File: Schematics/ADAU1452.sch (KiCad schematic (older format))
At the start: 99 parts, among them CN201 COAX, P201 CONN_2x1, P203 CONN_6X2, P204 CONN_6x1, SW202 SWITCH, U201 ADAU1452WBCPZ, U202 ADM13307-5ARZ, U203 25AA1024, X201 24M576

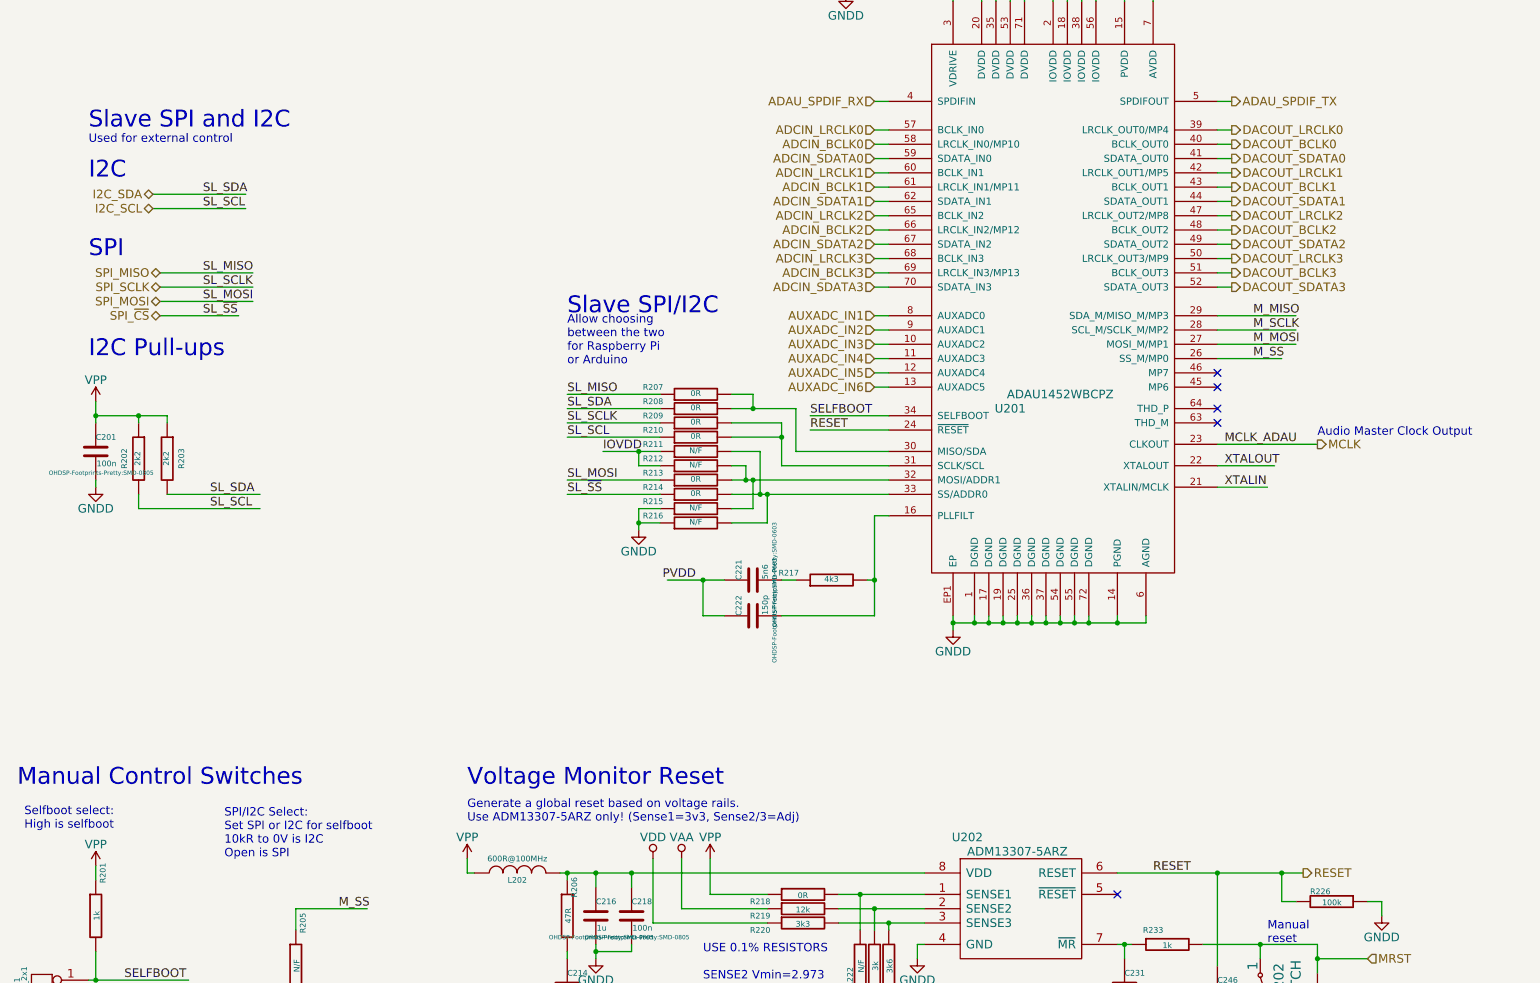
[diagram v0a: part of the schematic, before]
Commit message: WIP
Removed Slave SPI as only really need I2C
Should free up some space on the board.
May look to change U.fl to SMA
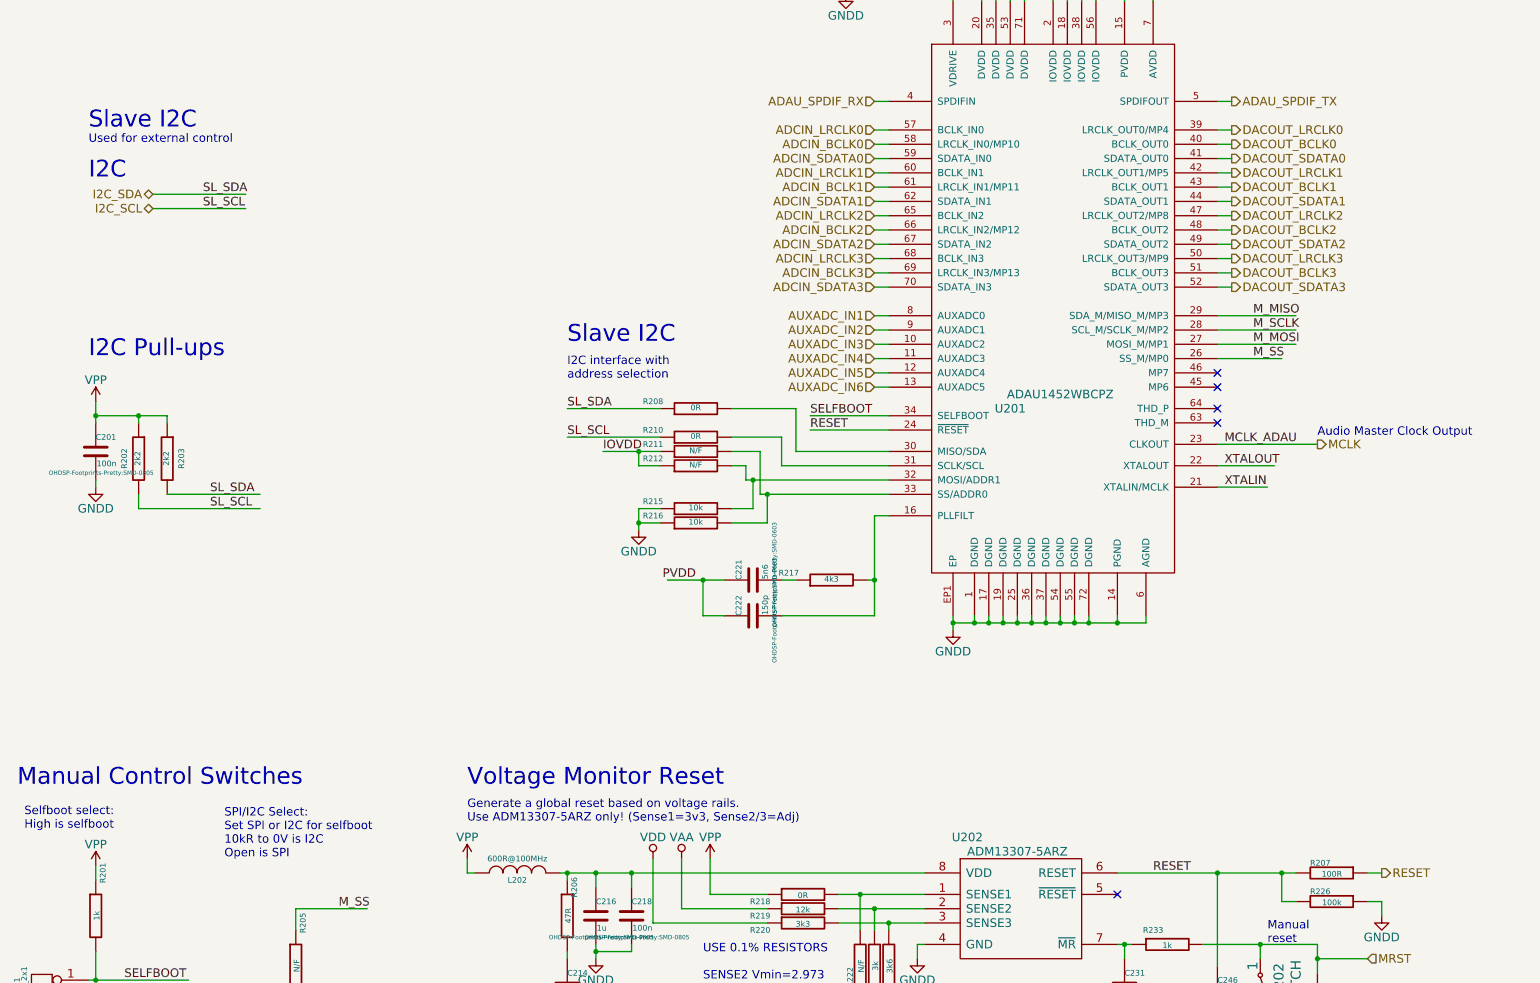
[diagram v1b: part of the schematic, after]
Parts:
- removed R209, R213, R214: 0R, OHDSP-Footprints-Pretty:SMD-0805, symbol R
- R207: value 0R -> 100R
- R215, R216: value N/F -> 10k
- U203: footprint OHDSP-Footprints-Pretty:IC_DIP_8 -> OHDSP-Footprints-Pretty:IC_SOIC_8
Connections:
- net labels removed: SL_MISO, SL_MOSI, SL_SCLK, SL_~SS, SPI_MISO, SPI_MOSI, SPI_SCLK, SPI_~CS
- wire segments 327 -> 317
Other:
- note added: "I2C interface with \naddress selection"
- note added: "Slave I2C"
- note removed: "Allow choosing\nbetween the two\nfor Raspberry Pi\nor Arduino"
- note removed: "SPI"
- note removed: "Slave SPI and I2C"
- note removed: "Slave SPI/I2C"
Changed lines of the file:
@@
 Text Notes 11450 4400 0    118  ~ 0
 SPI EEPROM
-Text Label 4500 6150 0    60   ~ 0
-SL_MISO
-Text Label 4500 6350 0    60   ~ 0
-SL_SCLK
-Text Label 4500 6850 0    60   ~ 0
-SL_~SS
-Text Label 4500 6750 0    60   ~ 0
-SL_MOSI
 $Comp
 L C C222
@@
 F 0 "U203" H 13940 5690 60  0000 C CNN
 F 1 "25AA1024" H 14050 5600 60  0000 C CNN
-F 2 "OHDSP-Footprints-Pretty:IC_DIP_8" H 13700 5550 60  0001 C CNN
+F 2 "OHDSP-Footprints-Pretty:IC_SOIC_8" H 13700 5550 60  0001 C CNN
 F 3 "" H 13700 5550 60  0000 C CNN
 	1    13600 5450
@@
 F 3 "~" H 5400 6250 30  0000 C CNN
 	1    5400 6250
-	0    -1   -1   0
-$EndComp
-$Comp
-L R R207
-U 1 1 54E23425
-P 5400 6150
-F 0 "R207" V 5450 6450 40  0000 C CNN
-F 1 "0R" V 5407 6151 40  0000 C CNN
-F 2 "OHDSP-Footprints-Pretty:SMD-0805" V 5330 6150 30  0001 C CNN
-F 3 "~" H 5400 6150 30  0000 C CNN
-	1    5400 6150
-	0    -1   -1   0
-$EndComp
-$Comp
-L R R209
-U 1 1 54E23533
-P 5400 6350
-F 0 "R209" V 5450 6650 40  0000 C CNN
-F 1 "0R" V 5407 6351 40  0000 C CNN
-F 2 "OHDSP-Footprints-Pretty:SMD-0805" V 5330 6350 30  0001 C CNN
-F 3 "~" H 5400 6350 30  0000 C CNN
-	1    5400 6350
 	0    -1   -1   0
 $EndComp
@@
 Text HLabel 6650 6100 0    60   Input ~ 0
 AUXADC_IN6
-Text Label 1950 5300 0    60   ~ 0
-SL_MISO
 Text Label 1950 4750 0    60   ~ 0
 SL_SDA
-Text Label 1950 5400 0    60   ~ 0
-SL_SCLK
 Text Label 1950 4850 0    60   ~ 0
 SL_SCL
-Text Label 1950 5500 0    60   ~ 0
-SL_MOSI
-Text Label 1950 5600 0    60   ~ 0
-SL_~SS
 Text HLabel 1600 4850 0    60   BiDi ~ 0
 I2C_SCL
 Text HLabel 1600 4750 0    60   BiDi ~ 0
 I2C_SDA
-Text HLabel 1650 5300 0    60   BiDi ~ 0
-SPI_MISO
-Text HLabel 1650 5400 0    60   BiDi ~ 0
-SPI_SCLK
-Text HLabel 1650 5500 0    60   BiDi ~ 0
-SPI_MOSI
-Text HLabel 1650 5600 0    60   BiDi ~ 0
-SPI_~CS
 Text Notes 1150 4650 0    118  ~ 0
 I2C
-Text Notes 1150 5200 0    118  ~ 0
-SPI
 $Comp
 L VPP #PWR020
@@
 Allow for self boot\nUses master SPI
 Text Notes 1150 4300 0    118  ~ 0
-Slave SPI and I2C
+Slave I2C
 Text Notes 1150 4400 0    59   ~ 0
 Used for external control
-$Comp
-L R R213
-U 1 1 54E3266A
-P 5400 6750
-F 0 "R213" V 5450 7050 40  0000 C CNN
-F 1 "0R" V 5407 6751 40  0000 C CNN
-F 2 "OHDSP-Footprints-Pretty:SMD-0805" V 5330 6750 30  0001 C CNN
-F 3 "~" H 5400 6750 30  0000 C CNN
-	1    5400 6750
-	0    -1   -1   0
-$EndComp
-$Comp
-L R R214
-U 1 1 54E326E9
-P 5400 6850
-F 0 "R214" V 5450 7150 40  0000 C CNN
-F 1 "0R" V 5407 6851 40  0000 C CNN
-F 2 "OHDSP-Footprints-Pretty:SMD-0805" V 5330 6850 30  0001 C CNN
-F 3 "~" H 5400 6850 30  0000 C CNN
-	1    5400 6850
-	0    -1   -1   0
-$EndComp
 $Comp
 L R R212
@@
 P 5400 6950
 F 0 "R215" V 5450 7250 40  0000 C CNN
-F 1 "N/F" V 5407 6951 40  0000 C CNN
+F 1 "10k" V 5407 6951 40  0000 C CNN
 F 2 "OHDSP-Footprints-Pretty:SMD-0805" V 5330 6950 30  0001 C CNN
 F 3 "~" H 5400 6950 30  0000 C CNN
@@
 P 5400 7050
 F 0 "R216" V 5450 7350 40  0000 C CNN
-F 1 "N/F" V 5407 7051 40  0000 C CNN
+F 1 "10k" V 5407 7051 40  0000 C CNN
 F 2 "OHDSP-Footprints-Pretty:SMD-0805" V 5330 7050 30  0001 C CNN
 F 3 "~" H 5400 7050 30  0000 C CNN
@@
 	1    0    0    -1
 $EndComp
-Text Notes 4500 5600 0    118  ~ 0
-Slave SPI/I2C
-Text Notes 4500 5950 0    59   ~ 0
-Allow choosing\nbetween the two\nfor Raspberry Pi\nor Arduino
+Text Notes 4500 5800 0    118  ~ 0
+Slave I2C
+Text Notes 4500 6050 0    59   ~ 0
+I2C interface with \naddress selection
 $Comp
 L CONN_6X2 P203
@@
 	1    0    0    -1
 $EndComp
-Text HLabel 9650 9500 2    60   Output ~ 0
+Text HLabel 10200 9500 2    60   Output ~ 0
 RESET
 $Comp
@@
 	9050 5900 9500 5900
 Wire Wire Line
-	4500 6750 5150 6750
-Wire Wire Line
-	4500 6850 5150 6850
-Wire Wire Line
 	6100 7450 6000 7450
 Wire Wire Line
@@
 	1500 6950 2350 6950
 Wire Wire Line
-	5650 6150 5800 6150
-Wire Wire Line
-	5800 6150 5800 6250
-Connection ~ 5800 6250
-Wire Wire Line
 	5650 6450 6000 6450
 Wire Wire Line
-	5150 6150 4500 6150
-Wire Wire Line
 	4500 6250 5150 6250
-Wire Wire Line
-	5150 6350 4500 6350
 Wire Wire Line
 	4500 6450 5150 6450
@@
 Wire Wire Line
 	1600 4850 2250 4850
-Wire Wire Line
-	1650 5300 2300 5300
-Wire Wire Line
-	1650 5400 2300 5400
-Wire Wire Line
-	1650 5500 2300 5500
-Wire Wire Line
-	1650 5600 2200 5600
 Connection ~ 1200 6300
 Wire Wire Line
@@
 	9050 6800 9400 6800
 Wire Wire Line
-	5650 6350 6000 6350
-Wire Wire Line
-	6000 6350 6000 6650
-Wire Wire Line
 	5650 6250 6100 6250
 Wire Wire Line
@@
 Wire Wire Line
 	6000 6650 6750 6650
-Connection ~ 6000 6450
-Wire Wire Line
-	5650 6750 6750 6750
-Wire Wire Line
-	5650 6850 6750 6850
 Wire Wire Line
 	4750 6550 5150 6550
@@
 Wire Wire Line
 	5750 6650 5750 6750
-Connection ~ 5750 6750
 Wire Wire Line
 	5650 6550 5850 6550
 Wire Wire Line
 	5850 6550 5850 6850
-Connection ~ 5850 6850
 Wire Wire Line
 	5650 6950 5800 6950
@@
 	14750 4850 15050 4850
 Wire Wire Line
-	8350 9500 9650 9500
+	8350 9500 9600 9500
 Wire Wire Line
 	9350 10100 9350 10000
@@
 	9050 10150 9050 9500
 Connection ~ 9050 9500
+Wire Wire Line
+	6000 6450 6000 6650
+Wire Wire Line
+	5750 6750 6750 6750
+Wire Wire Line
+	5850 6850 6750 6850
+$Comp
+L R R207
+U 1 1 551B9D0B
+P 9850 9500
+F 0 "R207" V 9780 9420 40  0000 C CNN
+F 1 "100R" V 9857 9501 40  0000 C CNN
+F 2 "OHDSP-Footprints-Pretty:SMD-0805" V 9780 9500 30  0001 C CNN
+F 3 "~" H 9850 9500 30  0000 C CNN
+	1    9850 9500
+	0    1    1    0
+$EndComp
+Wire Wire Line
+	10100 9500 10200 9500
 $EndSCHEMATC

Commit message: WIP
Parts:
- added C247: 100n, OHDSP-Footprints-Pretty:SMD-0805, symbol C
- R205: value N/F -> 100R
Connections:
- net labels added: DSP_RESET, GLB_RESET, MAN_RST_IN
- net labels removed: MRST, RESET
- wire segments 317 -> 319
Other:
- note added: "Selfboot Switch"
- note removed: "Manual Control Switches"
- note removed: "SPI/I2C Select:\nSet SPI or I2C for selfboot\n10kR to 0V is I2C\nOpen is SPI"
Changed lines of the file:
@@
 SELFBOOT
 Text Label 6200 6400 0    60   ~ 0
-RESET
+DSP_RESET
 Text Label 6200 6300 0    60   ~ 0
 SELFBOOT
 Text Notes 650  8900 0    118  ~ 0
-Manual Control Switches
+Selfboot Switch
 Text Notes 700  9200 0    59   ~ 0
 Selfboot select:\nHigh is selfboot
 Text Notes 3800 9150 0    59   ~ 0
 Generate a global reset based on voltage rails.\nUse ADM13307-5ARZ only! (Sense1=3v3, Sense2/3=Adj)
-$Comp
-L GNDD #PWR012
-U 1 1 54DBCD24
-P 2600 10500
-F 0 "#PWR012" H 2600 10250 60  0001 C CNN
-F 1 "GNDD" H 2600 10350 60  0000 C CNN
-F 2 "" H 2600 10500 60  0000 C CNN
-F 3 "" H 2600 10500 60  0000 C CNN
-	1    2600 10500
-	1    0    0    -1
-$EndComp
-Text Notes 2100 9400 0    59   ~ 0
-SPI/I2C Select:\nSet SPI or I2C for selfboot\n10kR to 0V is I2C\nOpen is SPI
-$Comp
-L R R205
-U 1 1 54DBE1BF
-P 2600 10150
-F 0 "R205" V 2650 10450 40  0000 C CNN
-F 1 "N/F" V 2607 10151 40  0000 C CNN
-F 2 "OHDSP-Footprints-Pretty:SMD-0805" V 2530 10150 30  0001 C CNN
-F 3 "~" H 2600 10150 30  0000 C CNN
-	1    2600 10150
-	1    0    0    -1
-$EndComp
 Text Label 9300 5900 0    60   ~ 0
 M_SS
@@
 $EndComp
 $Comp
-L GNDD #PWR013
+L GNDD #PWR012
 U 1 1 54DF7B4A
 P 10200 9800
-F 0 "#PWR013" H 10200 9550 60  0001 C CNN
+F 0 "#PWR012" H 10200 9550 60  0001 C CNN
 F 1 "GNDD" H 10200 9650 60  0000 C CNN
 F 2 "" H 10200 9800 60  0000 C CNN
@@
 $EndComp
 $Comp
-L GNDD #PWR014
+L GNDD #PWR013
 U 1 1 54DFF973
 P 15100 5950
-F 0 "#PWR014" H 15100 5700 60  0001 C CNN
+F 0 "#PWR013" H 15100 5700 60  0001 C CNN
 F 1 "GNDD" H 15100 5800 60  0000 C CNN
 F 2 "" H 15100 5950 60  0000 C CNN
@@
 $EndComp
 $Comp
-L GNDD #PWR015
+L GNDD #PWR014
 U 1 1 54E000FF
 P 12700 5950
-F 0 "#PWR015" H 12700 5700 60  0001 C CNN
+F 0 "#PWR014" H 12700 5700 60  0001 C CNN
 F 1 "GNDD" H 12700 5800 60  0000 C CNN
 F 2 "" H 12700 5950 60  0000 C CNN
@@
 $EndComp
 $Comp
-L GNDD #PWR016
+L GNDD #PWR015
 U 1 1 54E277D2
 P 1200 6800
-F 0 "#PWR016" H 1200 6550 60  0001 C CNN
+F 0 "#PWR015" H 1200 6550 60  0001 C CNN
 F 1 "GNDD" H 1200 6650 60  0000 C CNN
 F 2 "" H 1200 6800 60  0000 C CNN
@@
 $EndComp
 $Comp
-L GNDD #PWR017
+L GNDD #PWR016
 U 1 1 54E2D7D3
 P 12950 9500
-F 0 "#PWR017" H 12950 9250 60  0001 C CNN
+F 0 "#PWR016" H 12950 9250 60  0001 C CNN
 F 1 "GNDD" H 12950 9350 60  0000 C CNN
 F 2 "" H 12950 9500 60  0000 C CNN
@@
 $EndComp
 $Comp
-L GNDD #PWR018
+L GNDD #PWR017
 U 1 1 54E2D862
 P 13750 9500
-F 0 "#PWR018" H 13750 9250 60  0001 C CNN
+F 0 "#PWR017" H 13750 9250 60  0001 C CNN
 F 1 "GNDD" H 13750 9350 60  0000 C CNN
 F 2 "" H 13750 9500 60  0000 C CNN
@@
 $EndComp
 $Comp
-L GNDD #PWR019
+L GNDD #PWR018
 U 1 1 54E3B3FE
 P 15300 8850
-F 0 "#PWR019" H 15300 8600 60  0001 C CNN
+F 0 "#PWR018" H 15300 8600 60  0001 C CNN
 F 1 "GNDD" H 15300 8700 60  0000 C CNN
 F 2 "" H 15300 8850 60  0000 C CNN
@@
 I2C
 $Comp
-L VPP #PWR020
+L VPP #PWR019
 U 1 1 54E57AC0
 P 1200 6200
-F 0 "#PWR020" H 1200 6050 60  0001 C CNN
+F 0 "#PWR019" H 1200 6050 60  0001 C CNN
 F 1 "VPP" H 1200 6350 60  0000 C CNN
 F 2 "" H 1200 6200 60  0000 C CNN
@@
 $EndComp
 $Comp
-L GNDD #PWR021
+L GNDD #PWR020
 U 1 1 54E3539E
 P 5000 7100
-F 0 "#PWR021" H 5000 6850 60  0001 C CNN
+F 0 "#PWR020" H 5000 6850 60  0001 C CNN
 F 1 "GNDD" H 5000 6950 60  0000 C CNN
 F 2 "" H 5000 7100 60  0000 C CNN
@@
 EE_SI
 $Comp
-L GNDD #PWR022
+L GNDD #PWR021
 U 1 1 54E3FA17
 P 11700 5950
-F 0 "#PWR022" H 11700 5700 60  0001 C CNN
+F 0 "#PWR021" H 11700 5700 60  0001 C CNN
 F 1 "GNDD" H 11700 5800 60  0000 C CNN
 F 2 "" H 11700 5950 60  0000 C CNN
@@
 $EndComp
 $Comp
-L GNDD #PWR023
+L GNDD #PWR022
 U 1 1 54E400D8
 P 13550 5850
-F 0 "#PWR023" H 13550 5600 60  0001 C CNN
+F 0 "#PWR022" H 13550 5600 60  0001 C CNN
 F 1 "GNDD" H 13550 5700 60  0000 C CNN
 F 2 "" H 13550 5850 60  0000 C CNN
@@
 $EndComp
 $Comp
-L VPP #PWR024
+L VPP #PWR023
 U 1 1 54E4057B
 P 11700 5350
-F 0 "#PWR024" H 11700 5200 60  0001 C CNN
+F 0 "#PWR023" H 11700 5200 60  0001 C CNN
 F 1 "VPP" H 11700 5500 60  0000 C CNN
 F 2 "" H 11700 5350 60  0000 C CNN
@@
 $EndComp
 $Comp
-L GNDD #PWR025
+L GNDD #PWR024
 U 1 1 54E66110
 P 15400 5950
-F 0 "#PWR025" H 15400 5700 60  0001 C CNN
+F 0 "#PWR024" H 15400 5700 60  0001 C CNN
 F 1 "GNDD" H 15400 5800 60  0000 C CNN
 F 2 "" H 15400 5950 60  0000 C CNN
@@
 $EndComp
 $Comp
-L GNDD #PWR026
+L GNDD #PWR025
 U 1 1 54E793EE
 P 15000 5100
-F 0 "#PWR026" H 15000 4850 60  0001 C CNN
+F 0 "#PWR025" H 15000 4850 60  0001 C CNN
 F 1 "GNDD" H 15000 4950 60  0000 C CNN
 F 2 "" H 15000 5100 60  0000 C CNN
@@
 Programming\nHeader\n
 $Comp
-L VPP #PWR027
+L VPP #PWR026
 U 1 1 54E9D3D9
 P 1200 9450
-F 0 "#PWR027" H 1200 9300 60  0001 C CNN
+F 0 "#PWR026" H 1200 9300 60  0001 C CNN
 F 1 "VPP" H 1200 9600 60  0000 C CNN
 F 2 "" H 1200 9450 60  0000 C CNN
@@
 $EndComp
 $Comp
-L GNDD #PWR028
+L GNDD #PWR027
 U 1 1 54EA0E15
 P 9350 10550
-F 0 "#PWR028" H 9350 10300 60  0001 C CNN
+F 0 "#PWR027" H 9350 10300 60  0001 C CNN
 F 1 "GNDD" H 9350 10400 60  0000 C CNN
 F 2 "" H 9350 10550 60  0000 C CNN
@@
 $EndComp
 $Comp
-L GNDD #PWR029
+L GNDD #PWR028
 U 1 1 54EA141D
 P 8400 10550
-F 0 "#PWR029" H 8400 10300 60  0001 C CNN
+F 0 "#PWR028" H 8400 10300 60  0001 C CNN
 F 1 "GNDD" H 8400 10400 60  0000 C CNN
 F 2 "" H 8400 10550 60  0000 C CNN
@@
 $EndComp
 $Comp
-L GNDD #PWR030
+L GNDD #PWR029
 U 1 1 54EA28F6
 P 4500 10550
-F 0 "#PWR030" H 4500 10300 60  0001 C CNN
+F 0 "#PWR029" H 4500 10300 60  0001 C CNN
 F 1 "GNDD" H 4500 10400 60  0000 C CNN
 F 2 "" H 4500 10550 60  0000 C CNN
@@
 $EndComp
 $Comp
-L GNDD #PWR031
+L GNDD #PWR030
 U 1 1 54EA2F14
 P 4700 10100
-F 0 "#PWR031" H 4700 9850 60  0001 C CNN
+F 0 "#PWR030" H 4700 9850 60  0001 C CNN
 F 1 "GNDD" H 4700 9950 60  0000 C CNN
 F 2 "" H 4700 10100 60  0000 C CNN
@@
 $EndComp
 $Comp
-L GNDD #PWR032
+L GNDD #PWR031
 U 1 1 54EA451E
 P 6950 10100
-F 0 "#PWR032" H 6950 9850 60  0001 C CNN
+F 0 "#PWR031" H 6950 9850 60  0001 C CNN
 F 1 "GNDD" H 6950 9950 60  0000 C CNN
 F 2 "" H 6950 10100 60  0000 C CNN
@@
 $EndComp
 $Comp
-L GNDD #PWR033
+L GNDD #PWR032
 U 1 1 54EA6A23
 P 6750 10550
-F 0 "#PWR033" H 6750 10300 60  0001 C CNN
+F 0 "#PWR032" H 6750 10300 60  0001 C CNN
 F 1 "GNDD" H 6750 10400 60  0000 C CNN
 F 2 "" H 6750 10550 60  0000 C CNN
@@
 $EndComp
 $Comp
-L VDD #PWR034
+L VDD #PWR033
 U 1 1 54EA83B7
 P 5100 9400
-F 0 "#PWR034" H 5100 9250 60  0001 C CNN
+F 0 "#PWR033" H 5100 9250 60  0001 C CNN
 F 1 "VDD" H 5100 9550 60  0000 C CNN
 F 2 "" H 5100 9400 60  0000 C CNN
@@
 $EndComp
 $Comp
-L VPP #PWR035
+L VPP #PWR034
 U 1 1 54EA842E
 P 5500 9400
-F 0 "#PWR035" H 5500 9250 60  0001 C CNN
+F 0 "#PWR034" H 5500 9250 60  0001 C CNN
 F 1 "VPP" H 5500 9550 60  0000 C CNN
 F 2 "" H 5500 9400 60  0000 C CNN
@@
 $EndComp
 $Comp
-L VAA #PWR036
+L VAA #PWR035
 U 1 1 54EA84A5
 P 5300 9400
-F 0 "#PWR036" H 5300 9250 60  0001 C CNN
+F 0 "#PWR035" H 5300 9250 60  0001 C CNN
 F 1 "VAA" H 5300 9550 60  0000 C CNN
 F 2 "" H 5300 9400 60  0000 C CNN
@@
 $EndComp
 Text HLabel 10200 9500 2    60   Output ~ 0
-RESET
+GLB_RESET
 $Comp
 L R R219
@@
 $EndComp
 $Comp
-L VPP #PWR037
+L VPP #PWR036
 U 1 1 54E404E0
 P 3800 9400
-F 0 "#PWR037" H 3800 9250 60  0001 C CNN
+F 0 "#PWR036" H 3800 9250 60  0001 C CNN
 F 1 "VPP" H 3800 9550 60  0000 C CNN
 F 2 "" H 3800 9400 60  0000 C CNN
@@
 $EndComp
 $Comp
-L GNDD #PWR038
+L GNDD #PWR037
 U 1 1 54EF27F5
 P 14200 9300
-F 0 "#PWR038" H 14200 9050 60  0001 C CNN
+F 0 "#PWR037" H 14200 9050 60  0001 C CNN
 F 1 "GNDD" H 14200 9150 60  0000 C CNN
 F 2 "" H 14200 9300 60  0000 C CNN
@@
 	6750 6400 6200 6400
 Wire Wire Line
-	2600 9750 3100 9750
-Wire Wire Line
-	2600 9750 2600 9900
-Wire Wire Line
-	2600 10400 2600 10500
-Wire Wire Line
 	9050 5900 9500 5900
 Wire Wire Line
@@
 $EndComp
 $Comp
-L GNDD #PWR039
+L GNDD #PWR038
 U 1 1 54F4C05D
 P 13250 1750
-F 0 "#PWR039" H 13250 1500 60  0001 C CNN
+F 0 "#PWR038" H 13250 1500 60  0001 C CNN
 F 1 "GNDD" H 13250 1600 60  0000 C CNN
 F 2 "" H 13250 1750 60  0000 C CNN
@@
 	13250 1750 13250 1700
 Connection ~ 13250 1050
-Text Label 2900 9750 0    60   ~ 0
-M_SS
 Text HLabel 10100 10100 2    60   Input ~ 0
-MRST
+MAN_RST_IN
 Wire Wire Line
 	10100 10100 9750 10100
@@
 $EndComp
 $Comp
-L GNDD #PWR040
+L GNDD #PWR039
 U 1 1 54FF363C
 P 9750 10650
-F 0 "#PWR040" H 9750 10400 60  0001 C CNN
+F 0 "#PWR039" H 9750 10400 60  0001 C CNN
 F 1 "GNDD" H 9750 10500 60  0000 C CNN
 F 2 "" H 9750 10650 60  0000 C CNN
@@
 Wire Wire Line
 	9750 10650 9750 10600
-Text Label 8600 9500 0    60   ~ 0
-RESET
 $Comp
 L C C246
@@
 $EndComp
 $Comp
-L GNDD #PWR041
+L GNDD #PWR040
 U 1 1 54FF7C76
 P 9050 10600
-F 0 "#PWR041" H 9050 10350 60  0001 C CNN
+F 0 "#PWR040" H 9050 10350 60  0001 C CNN
 F 1 "GNDD" H 9050 10450 60  0000 C CNN
 F 2 "" H 9050 10600 60  0000 C CNN
@@
 Wire Wire Line
 	10100 9500 10200 9500
+$Comp
+L R R205
+U 1 1 551D8E6C
+P 9200 8650
+F 0 "R205" V 9130 8570 40  0000 C CNN
+F 1 "100R" V 9207 8651 40  0000 C CNN
+F 2 "OHDSP-Footprints-Pretty:SMD-0805" V 9130 8650 30  0001 C CNN
+F 3 "~" H 9200 8650 30  0000 C CNN
+	1    9200 8650
+	0    1    1    0
+$EndComp
+Text Label 10300 8650 2    60   ~ 0
+DSP_RESET
+Wire Wire Line
+	8950 8650 8650 8650
+Wire Wire Line
+	8650 8650 8650 9500
+Connection ~ 8650 9500
+$Comp
+L C C247
+U 1 1 551DA835
+P 10550 8950
+F 0 "C247" H 10550 9050 40  0000 L CNN
+F 1 "100n" H 10556 8865 40  0000 L CNN
+F 2 "OHDSP-Footprints-Pretty:SMD-0805" H 10588 8800 30  0000 C CNN
+F 3 "~" H 10550 8950 60  0000 C CNN
+	1    10550 8950
+	1    0    0    -1
+$EndComp
+Wire Wire Line
+	9450 8650 10550 8650
+Wire Wire Line
+	10550 8650 10550 8750
+$Comp
+L GNDD #PWR041
+U 1 1 551DB2BB
+P 10550 9200
+F 0 "#PWR041" H 10550 8950 60  0001 C CNN
+F 1 "GNDD" H 10550 9050 60  0000 C CNN
+F 2 "" H 10550 9200 60  0000 C CNN
+F 3 "" H 10550 9200 60  0000 C CNN
+	1    10550 9200
+	-1   0    0    -1
+$EndComp
+Wire Wire Line
+	10550 9200 10550 9150
 $EndSCHEMATC
